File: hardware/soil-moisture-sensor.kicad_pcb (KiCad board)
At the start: 2 copper layers, 185.3 x 23 mm, 23 parts, among them J1 AVR ISP, J2 FTDI, SW1 SW_Push, U1 ATmega328P-AU, U2 NRF24L01_Breakout, U3 ATSHA204A, Y1 Resonator

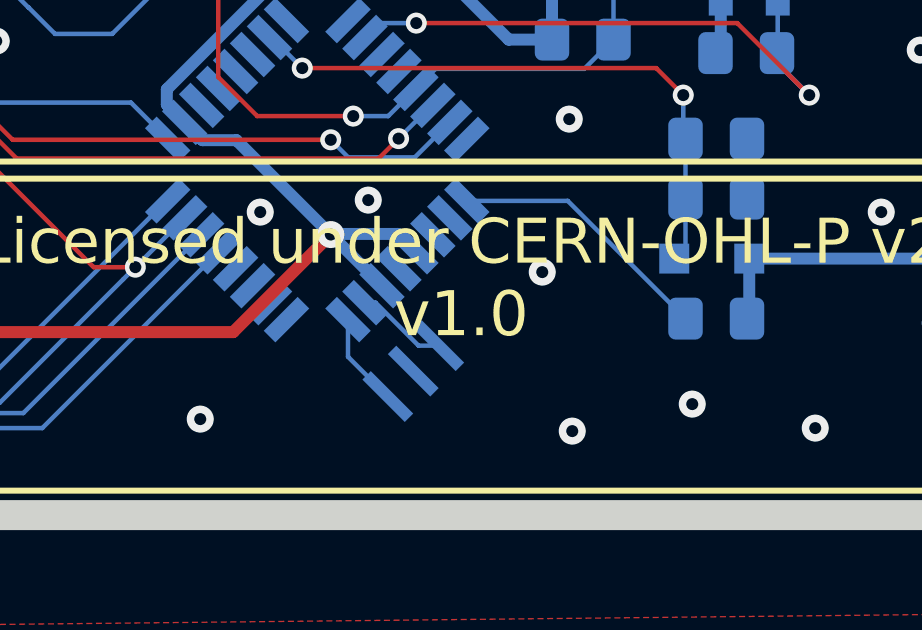
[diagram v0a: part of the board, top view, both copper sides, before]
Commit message: Add %%version%% and %%date%% placeholders
The '%%version%%' and '%%date%%' placeholders have been added to the
appropriate locations in the schematic and pcb file. They are
automatically replaced during a release with the correct version and
date of the release.
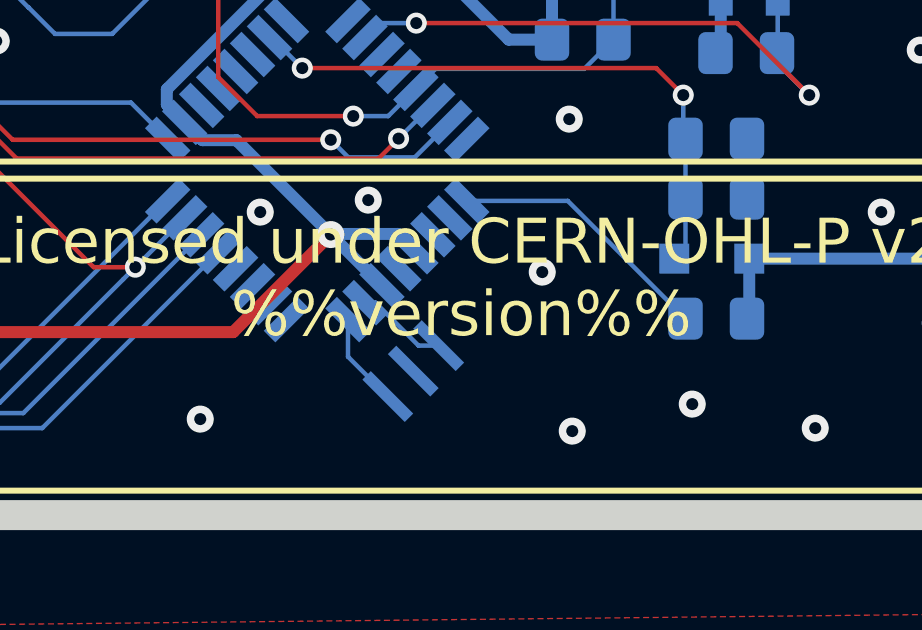
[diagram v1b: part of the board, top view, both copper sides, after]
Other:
- board text added: "Licensed under CERN-OHL-P v2 %%version%%"
- board text removed: "Licensed under CERN-OHL-P v2 v1.0"
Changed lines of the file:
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@@
-(kicad_pcb (version 20171130) (host pcbnew "(5.1.10)-1")
+(kicad_pcb (version 20171130) (host pcbnew "(5.1.12)-1")
   (general
     (thickness 1.6)
@@
   (page A4)
   (title_block
-    (date 2020-08-01)
-    (rev 1.0)
+    (date %%date%%)
+    (rev %%version%%)
   )
   (layers
@@
     )
   )
-  (gr_text "Licensed under CERN-OHL-P v2\nv1.0" (at 116.3 117.8) (layer F.SilkS)
+  (gr_text "Licensed under CERN-OHL-P v2\n%%version%%" (at 116.3 117.8) (layer F.SilkS)
     (effects (font (size 1.5 1.5) (thickness 0.3)))
   )
